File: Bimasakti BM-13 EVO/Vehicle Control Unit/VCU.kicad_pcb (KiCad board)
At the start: 2 copper layers, 68.1 x 36.8 mm, 5 parts, among them U1 SRV05-4

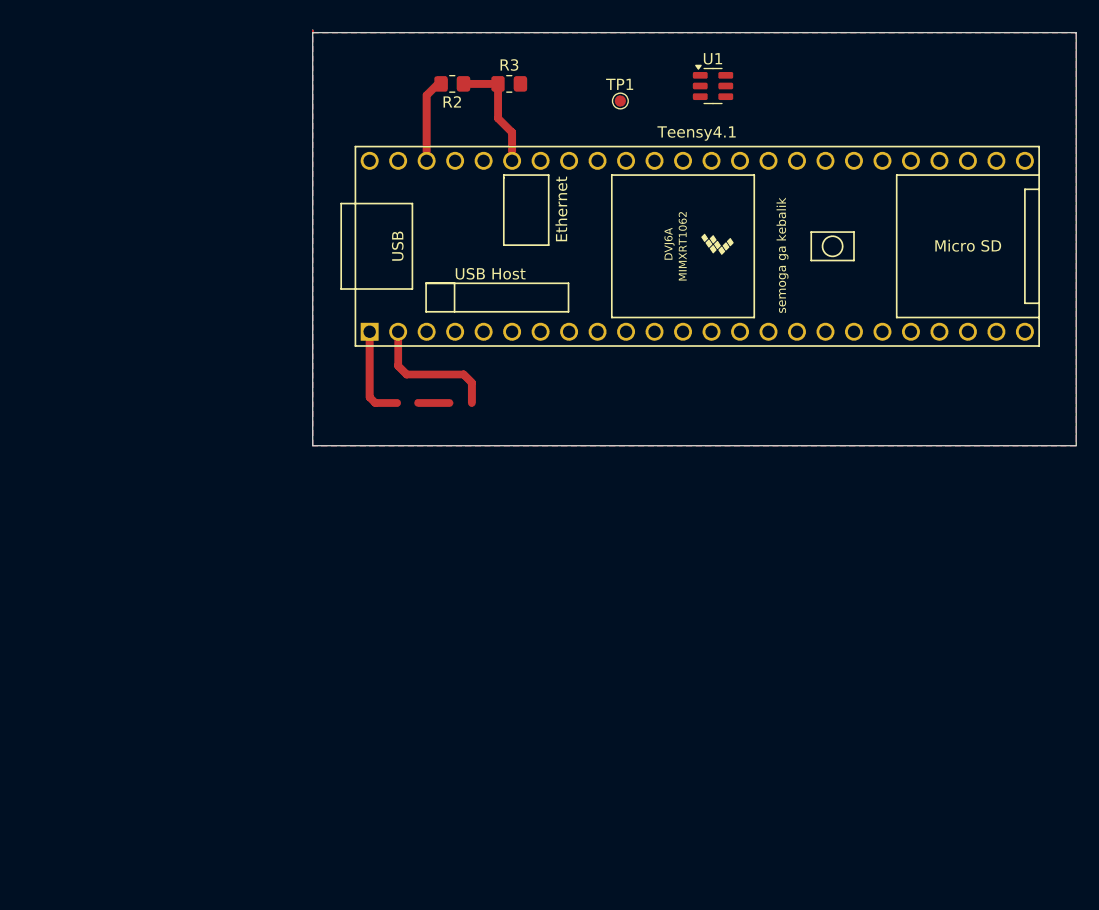
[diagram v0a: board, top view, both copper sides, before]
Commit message: add footprint library to project
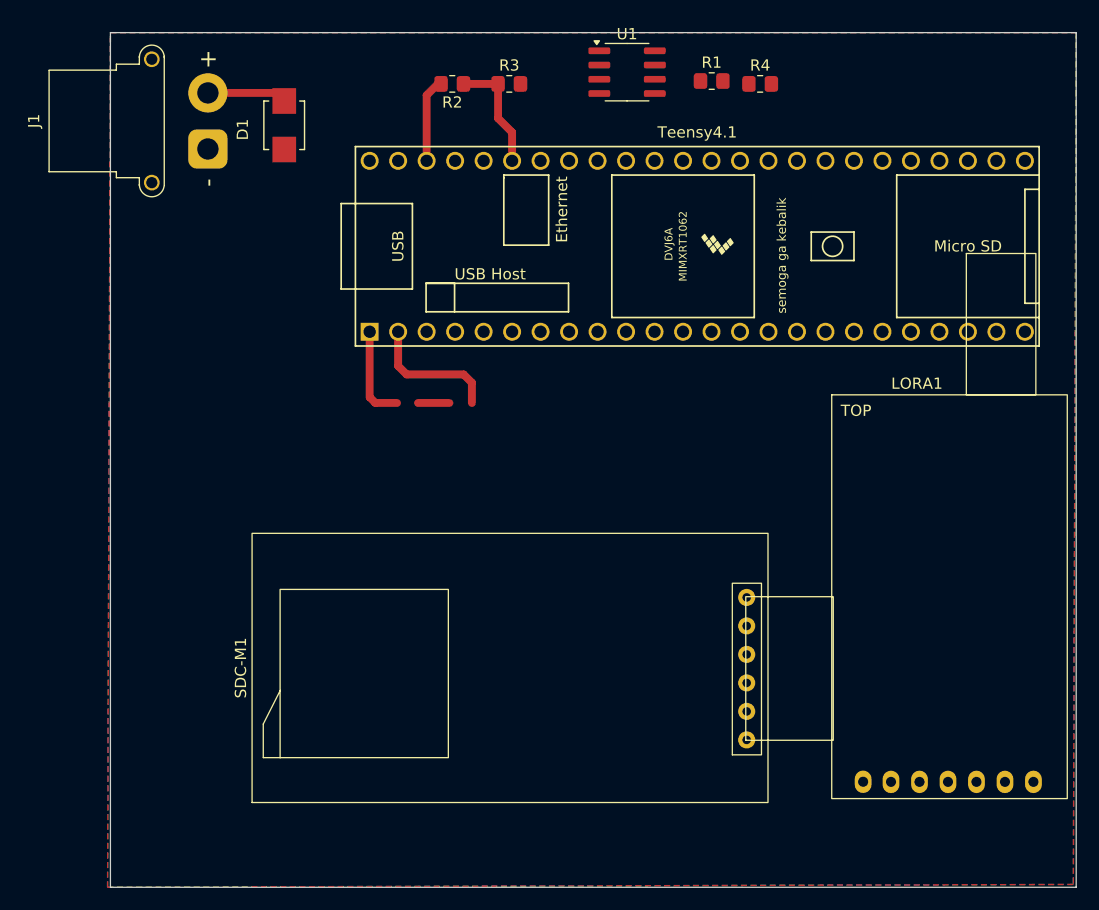
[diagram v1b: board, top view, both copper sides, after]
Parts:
- removed TP1: TestPoint, TestPoint:TestPoint_Pad_D1.0mm
- added D1: SMBJ12CA, TVS:DIOM4336X265N, F.Cu at (103.6, 62.6)
- added J1: Conn_01x02_Socket, Connector_AMASS:AMASS_XT30PW-F_1x02_P2.50mm_Horizontal, F.Cu at (96.8, 64.7)
- added LORA1: ~, Lora Module:E220-900T22D, F.Cu at (163.4, 104.6)
- added R1: 10K, Resistor_SMD:R_0805_2012Metric_Pad1.20x1.40mm_HandSolder, F.Cu at (141.7, 58.7)
- added R4: 120, Resistor_SMD:R_0805_2012Metric_Pad1.20x1.40mm_HandSolder, F.Cu at (146.1, 58.9)
- added SDC-M1: ~, SD card Module:SDCard, F.Cu at (123.8, 111.0)
- U1: value SRV05-4 -> MCP2551-I-SN; footprint Package_TO_SOT_SMD:SOT-23-6 -> Package_SO:SOIC-8_3.9x4.9mm_P1.27mm
- moved U1 7.76 mm to (134.2, 57.9)
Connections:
- Teensy4.1 pad 36: unconnected-(Teensy4.1-A0/TX3-Pad36) -> Net-(Teensy4.1-A0/TX3)
- Teensy4.1 pad 37: unconnected-(Teensy4.1-A1/RX3-Pad37) -> Net-(Teensy4.1-A1/RX3)
- U1 pad 1: unconnected-(U1-IO1-Pad1) -> Net-(Teensy4.1-A1/RX3)
- U1 pad 3: unconnected-(U1-IO2-Pad3) -> 3.3V
- U1 pad 4: unconnected-(U1-IO3-Pad4) -> Net-(Teensy4.1-A0/TX3)
- U1 pad 5: 3.3V -> unconnected-(U1-Vref-Pad5)
- U1 pad 6: unconnected-(U1-IO4-Pad6) -> Net-(U1-CANL)
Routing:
- net 3.3V: track 0.00 -> 6.63 mm
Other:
- board size 68.1 x 36.8 mm -> 86.1 x 76.2 mm

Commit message: Revert "add footprint library to project"
This reverts commit c2ea81f1652adadaa2769e08c07f448226fedb71.
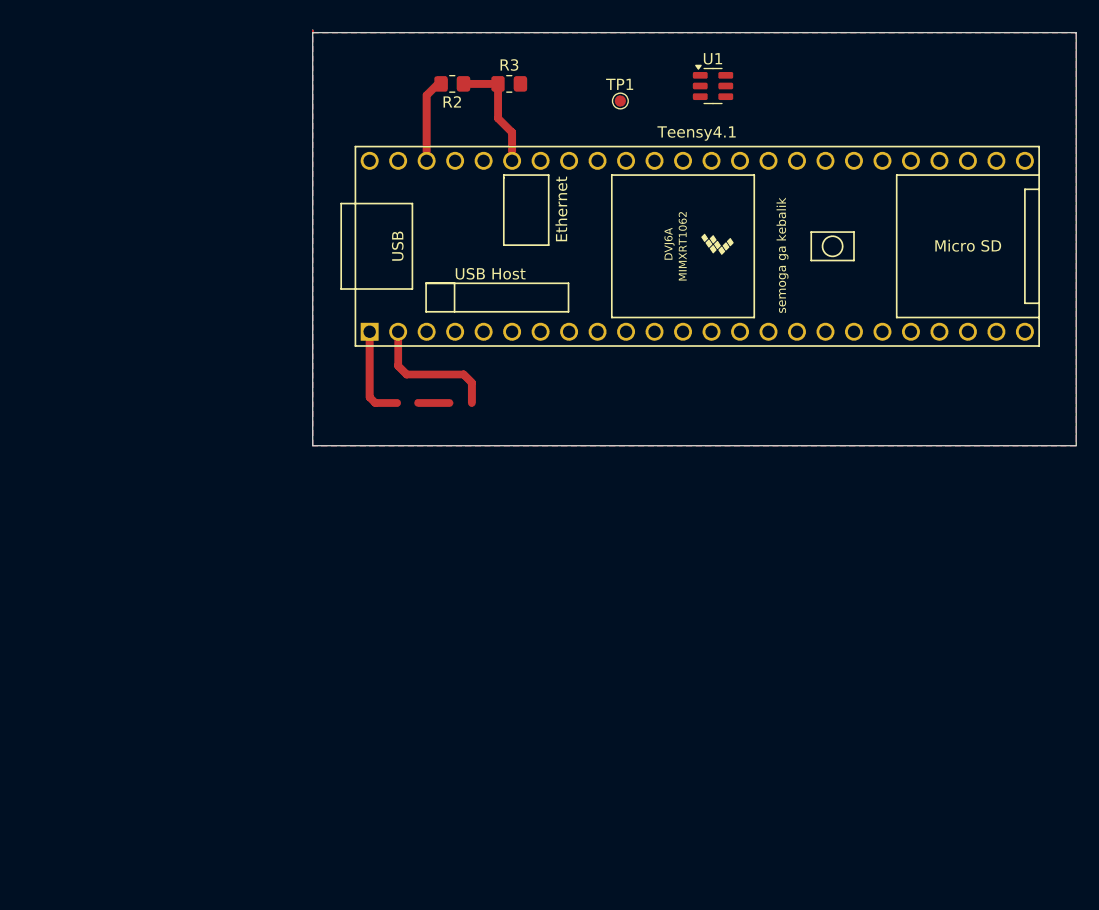
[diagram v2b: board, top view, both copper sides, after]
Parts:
- removed D1: SMBJ12CA, TVS:DIOM4336X265N
- removed J1: Conn_01x02_Socket, Connector_AMASS:AMASS_XT30PW-F_1x02_P2.50mm_Horizontal
- removed LORA1: ~, Lora Module:E220-900T22D
- removed R1: 10K, Resistor_SMD:R_0805_2012Metric_Pad1.20x1.40mm_HandSolder
- removed R4: 120, Resistor_SMD:R_0805_2012Metric_Pad1.20x1.40mm_HandSolder
- removed SDC-M1: ~, SD card Module:SDCard
- added TP1: TestPoint, TestPoint:TestPoint_Pad_D1.0mm, F.Cu at (133.6, 60.5)
- U1: value MCP2551-I-SN -> SRV05-4; footprint Package_SO:SOIC-8_3.9x4.9mm_P1.27mm -> Package_TO_SOT_SMD:SOT-23-6
- moved U1 7.76 mm to (141.9, 59.1)
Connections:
- Teensy4.1 pad 36: Net-(Teensy4.1-A0/TX3) -> unconnected-(Teensy4.1-A0/TX3-Pad36)
- Teensy4.1 pad 37: Net-(Teensy4.1-A1/RX3) -> unconnected-(Teensy4.1-A1/RX3-Pad37)
- U1 pad 1: Net-(Teensy4.1-A1/RX3) -> unconnected-(U1-IO1-Pad1)
- U1 pad 3: 3.3V -> unconnected-(U1-IO2-Pad3)
- U1 pad 4: Net-(Teensy4.1-A0/TX3) -> unconnected-(U1-IO3-Pad4)
- U1 pad 5: unconnected-(U1-Vref-Pad5) -> 3.3V
- U1 pad 6: Net-(U1-CANL) -> unconnected-(U1-IO4-Pad6)
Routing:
- net 3.3V: track 6.63 -> 0.00 mm
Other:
- board size 86.1 x 76.2 mm -> 68.1 x 36.8 mm
